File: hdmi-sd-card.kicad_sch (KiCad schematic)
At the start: 95 parts, among them J11 I-PEX_CABLINE-VS_1x20_20455-A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, J4 HDMI-A_WE_685119134923, J5 MicroSD_693071020811, Q18 BSS138PW, Q19 BSS138PW, Q21 BSS138PW, U10 TPD4E05U06QDQARQ1, U11 TPD4E05U06QDQARQ1, U37 TPD4E05U06QDQARQ1, U38 SN65DP159RGZR, U40 NVT4858_XQFN, U41 TPD4E05U06QDQARQ1, U42 M24C64-F_DFN8, U43 TPS2116DRLR, U44 TXS0102DQER, U47 TPD4E05U06QDQARQ1, U48 TPD4E05U06QDQARQ1

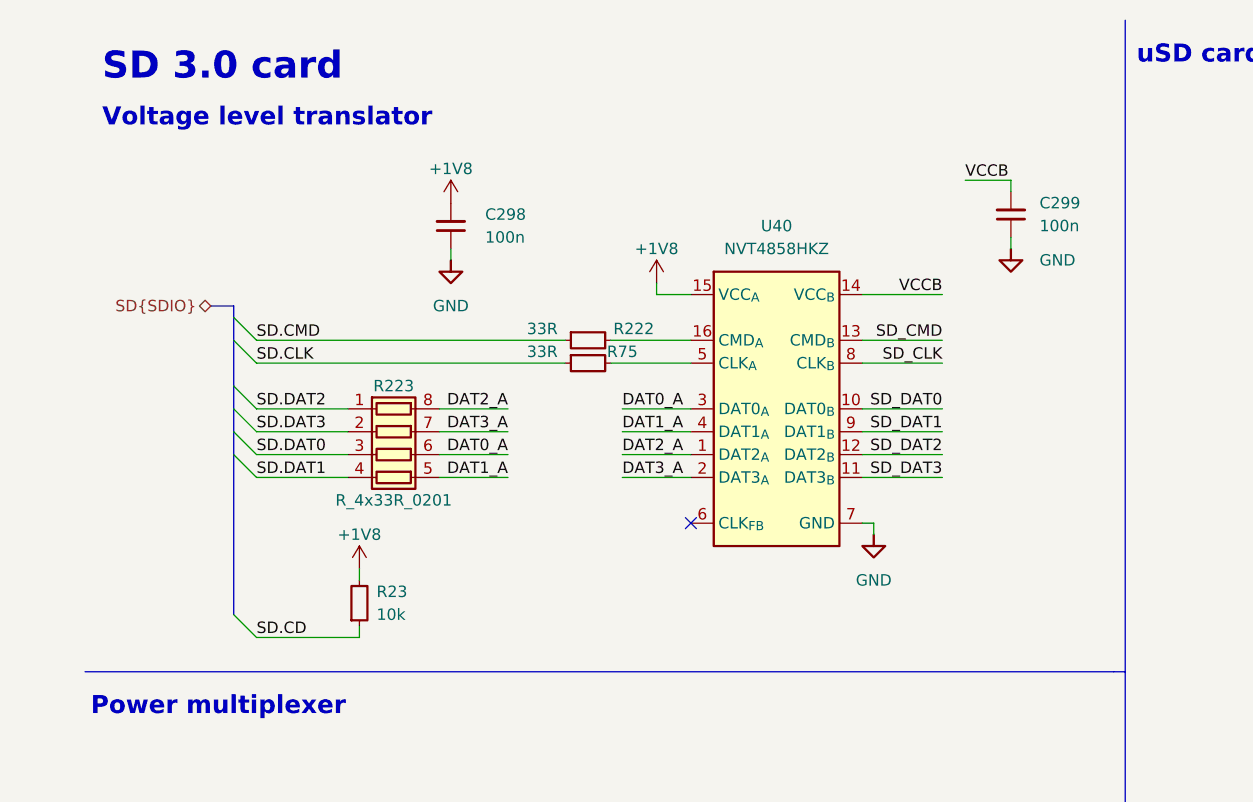
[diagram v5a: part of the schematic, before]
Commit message: [#68016] Remove series resistance from the SD card lanes
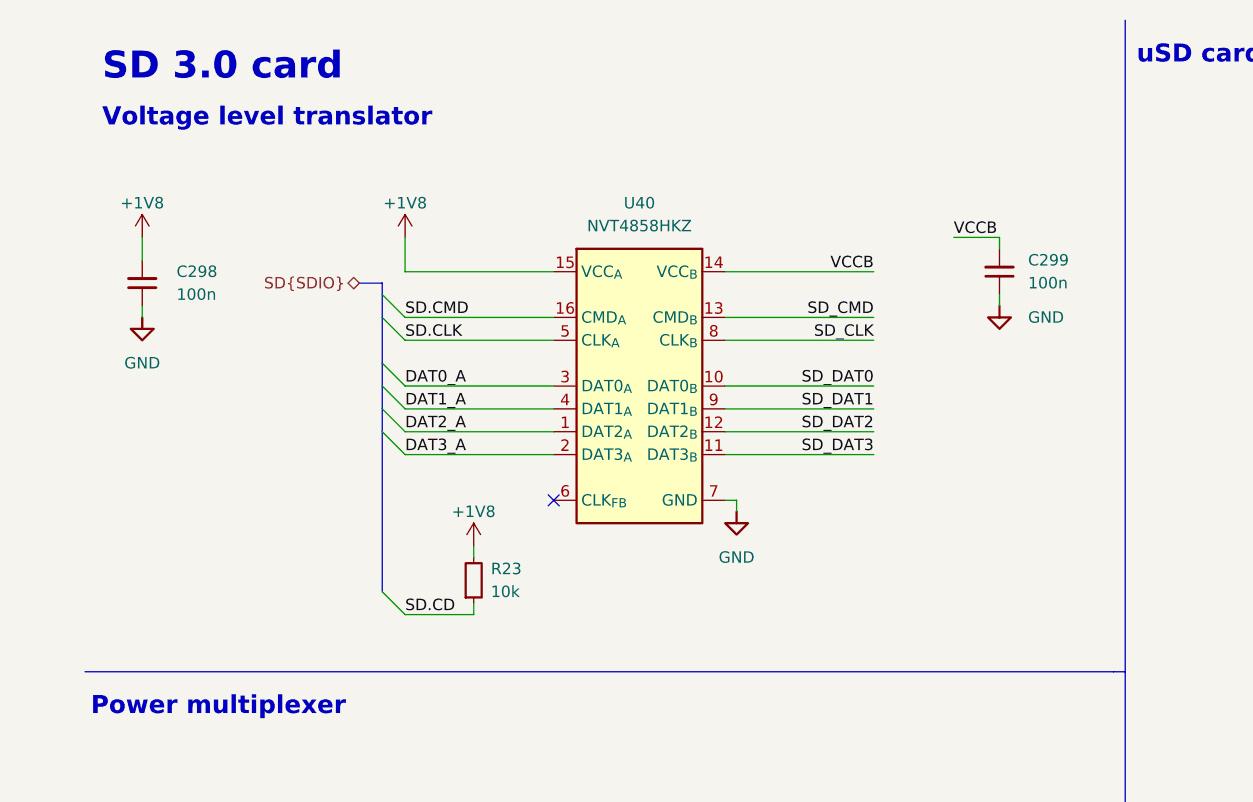
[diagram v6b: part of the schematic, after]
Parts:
- removed R222, R75: R_33R_0402, antmicro-footprints:R_0402_1005Metric, symbol antmicroResistors0402:R_33R_0402
- removed R223: R_4x33R_0201_array, antmicro-footprints:R_Array_4x0201_Panasonic_EXB18V, symbol antmicroResistorNetworksArrays:R_4x33R_0201_array
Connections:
- net SD.CLK: now also U40.5 (CLK_{A})
- net SD.CMD: now also U40.16 (CMD_{A})
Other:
- moved on the sheet: C298, C299, R23, U40

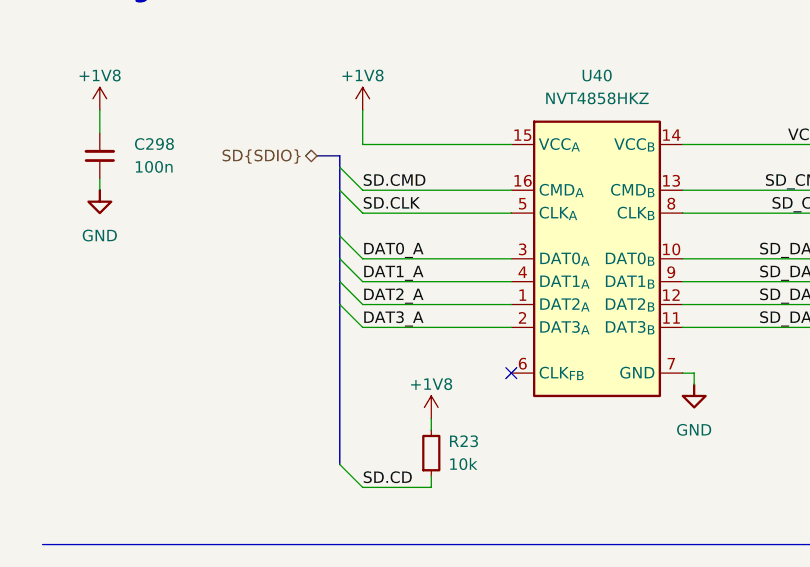
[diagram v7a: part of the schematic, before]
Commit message: [#67408] Update layout for I3C, SDcard and HDMI aux signals
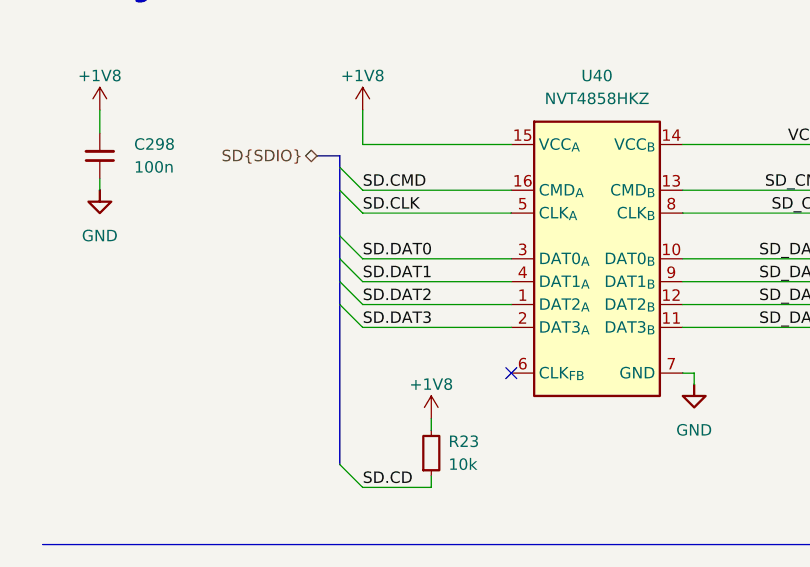
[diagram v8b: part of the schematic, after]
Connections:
- net DAT0_A renamed SD.DAT0
- net DAT1_A renamed SD.DAT1
- net DAT2_A renamed SD.DAT2
- net DAT3_A renamed SD.DAT3
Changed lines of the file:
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@@
     (effects (font (size 1.27 1.27)) (justify right bottom))
   )
-  (label "DAT1_A" (at 48.26 55.88 0) (fields_autoplaced)
+  (label "SD.DAT1" (at 48.26 55.88 0) (fields_autoplaced)
     (effects (font (size 1.27 1.27)) (justify left bottom))
   )
@@
     (effects (font (size 1.27 1.27)) (justify left bottom))
   )
-  (label "DAT3_A" (at 48.26 60.96 0) (fields_autoplaced)
+  (label "SD.DAT3" (at 48.26 60.96 0) (fields_autoplaced)
     (effects (font (size 1.27 1.27)) (justify left bottom))
   )
@@
     (effects (font (size 1.27 1.27)) (justify left bottom))
   )
-  (label "DAT0_A" (at 48.26 53.34 0) (fields_autoplaced)
+  (label "SD.DAT0" (at 48.26 53.34 0) (fields_autoplaced)
     (effects (font (size 1.27 1.27)) (justify left bottom))
   )
@@
     (effects (font (size 1.27 1.27)) (justify left bottom))
   )
-  (label "DAT2_A" (at 48.26 58.42 0) (fields_autoplaced)
+  (label "SD.DAT2" (at 48.26 58.42 0) (fields_autoplaced)
     (effects (font (size 1.27 1.27)) (justify left bottom))
   )
